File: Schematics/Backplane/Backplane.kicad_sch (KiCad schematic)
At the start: 0 parts

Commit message: First draft of schematic
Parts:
- added H1 (x2), H2 (x2), H3 (x2), H4 (x2): MountingHole, Footprints:Rod_Mounting_Hole_6.7564mm, symbol Mechanical:MountingHole
- added J1: Edge Connector (SLOT 1), footprints:AMPHENOL_10018784-10210TLF, symbol EdgeConnector:Stack Female Edge Connector
- added J2: Edge Connector (SLOT 2), footprints:AMPHENOL_10018784-10210TLF, symbol EdgeConnector:Stack Female Edge Connector
- added J3: Edge Connector (SLOT 3), footprints:AMPHENOL_10018784-10210TLF, symbol EdgeConnector:Stack Female Edge Connector
- added J4: Edge Connector (SLOT 4), footprints:AMPHENOL_10018784-10210TLF, symbol EdgeConnector:Stack Female Edge Connector
- added J5: Edge Connector (SLOT 5), footprints:AMPHENOL_10018784-10210TLF, symbol EdgeConnector:Stack Female Edge Connector
- added JP1: TOP_TERMINATION, symbol Jumper:Jumper_2_Bridged
- added JP2: BOT_TERMINATION, symbol Jumper:Jumper_2_Bridged
- added R1, R2: 120R, symbol Device:R
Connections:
- new net: JP2.1 (A), R2.1
- new net: JP1.1 (A), R1.1
- new net 3.3V_A: J1.A1 (3.3V_A), J1.A2 (3.3V_A), J2.A1 (3.3V_A), J2.A2 (3.3V_A), J3.A1 (3.3V_A), J3.A2 (3.3V_A), J4.A1 (3.3V_A), J4.A2 (3.3V_A), J5.A1 (3.3V_A), J5.A2 (3.3V_A)
- new net 3.3V_B: J1.A7 (3.3V_B), J1.A8 (3.3V_B), J2.A7 (3.3V_B), J2.A8 (3.3V_B), J3.A7 (3.3V_B), J3.A8 (3.3V_B), J4.A7 (3.3V_B), J4.A8 (3.3V_B), J5.A7 (3.3V_B), J5.A8 (3.3V_B)
- new net 5.0V_A: J1.A4 (5.0V_A), J1.A5 (5.0V_A), J2.A4 (5.0V_A), J2.A5 (5.0V_A), J3.A4 (5.0V_A), J3.A5 (5.0V_A), J4.A4 (5.0V_A), J4.A5 (5.0V_A), J5.A4 (5.0V_A), J5.A5 (5.0V_A)
- new net BATT_A: J1.B1 (BATT_A), J1.B2 (BATT_A), J1.B3 (BATT_A), J2.B1 (BATT_A), J2.B2 (BATT_A), J2.B3 (BATT_A), J3.B1 (BATT_A), J3.B2 (BATT_A), J3.B3 (BATT_A), J4.B1 (BATT_A), J4.B2 (BATT_A), J4.B3 (BATT_A), J5.B1 (BATT_A), J5.B2 (BATT_A), J5.B3 (BATT_A)
- new net BATT_B: J1.B7 (BATT_B), J1.B8 (BATT_B), J1.B9 (BATT_B), J2.B7 (BATT_B), J2.B8 (BATT_B), J2.B9 (BATT_B), J3.B7 (BATT_B), J3.B8 (BATT_B), J3.B9 (BATT_B), J4.B7 (BATT_B), J4.B8 (BATT_B), J4.B9 (BATT_B), J5.B7 (BATT_B), J5.B8 (BATT_B), J5.B9 (BATT_B)
- new net CAN_H: J1.B14 (CAN_H), J2.B14 (CAN_H), J3.B14 (CAN_H), J4.B14 (CAN_H), J5.B14 (CAN_H), JP1.2 (B), JP2.2 (B)
- new net CAN_L: J1.B13 (CAN_L), J2.B13 (CAN_L), J3.B13 (CAN_L), J4.B13 (CAN_L), J5.B13 (CAN_L), R1.2, R2.2
- new net GND1: J1.A3 (GND_A), J1.A6 (GND_A), J1.B4 (GND_A), J1.B5 (GND_A), J1.B6 (GND_A), J2.A3 (GND_A), J2.A6 (GND_A), J2.B4 (GND_A), J2.B5 (GND_A), J2.B6 (GND_A), J3.A3 (GND_A), J3.A6 (GND_A), J3.B4 (GND_A), J3.B5 (GND_A), J3.B6 (GND_A), J4.A3 (GND_A), J4.A6 (GND_A), J4.B4 (GND_A), J4.B5 (GND_A), J4.B6 (GND_A), J5.A3 (GND_A), J5.A6 (GND_A), J5.B4 (GND_A), J5.B5 (GND_A), J5.B6 (GND_A)
- new net GND2: J1.A12 (GND_B), J1.A9 (GND_B), J1.B10 (GND_B), J1.B11 (GND_B), J1.B12 (GND_B), J2.A12 (GND_B), J2.A9 (GND_B), J2.B10 (GND_B), J2.B11 (GND_B), J2.B12 (GND_B), J3.A12 (GND_B), J3.A9 (GND_B), J3.B10 (GND_B), J3.B11 (GND_B), J3.B12 (GND_B), J4.A12 (GND_B), J4.A9 (GND_B), J4.B10 (GND_B), J4.B11 (GND_B), J4.B12 (GND_B), J5.A12 (GND_B), J5.A9 (GND_B), J5.B10 (GND_B), J5.B11 (GND_B), J5.B12 (GND_B)
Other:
- note added: "1. WHAT SIZE MOUNTING HOLES? 2. EXPOSE DEBUG LEDS? 3. 4 LAYER OR 2 LAYER? 4. USE JLCPCB PCB ASSEMBLY?"
- note added: "CANBUS Termination"
- note added: "Mounting Holes"
- note added: "PASSTHROUGH?"

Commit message: Preliminary PCB design and layout
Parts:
- H1, H2, H3, H4: footprint Footprints:Rod_Mounting_Hole_6.7564mm -> MountingHole:MountingHole_3.2mm_M3_DIN965_Pad
- JP1, JP2: footprint (none) -> Jumper:SolderJumper-2_P1.3mm_Open_RoundedPad1.0x1.5mm
- R1, R2: footprint (none) -> Resistor_SMD:R_0805_2012Metric_Pad1.20x1.40mm_HandSolder
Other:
- note added: "1. EXPOSE DEBUG LEDS? 2. 4 LAYER OR 2 LAYER? 3. USE JLCPCB PCB ASSEMBLY? 4. NEED BETTER HOLE FOOTPRINTS?"
- note added: "DIMENSIONS NEED UPDATING"
- note removed: "1. WHAT SIZE MOUNTING HOLES? 2. EXPOSE DEBUG LEDS? 3. 4 LAYER OR 2 LAYER? 4. USE JLCPCB PCB ASSEMBLY?"
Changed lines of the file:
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@@
     (effects (font (size 1.27 1.27) (thickness 0.254) bold) (justify left bottom))
   )
-  (text "1. WHAT SIZE MOUNTING HOLES?\n2. EXPOSE DEBUG LEDS?\n3. 4 LAYER OR 2 LAYER?\n4. USE JLCPCB PCB ASSEMBLY?"
-    (at 21.59 166.37 0)
+  (text "DIMENSIONS NEED\nUPDATING" (at 308.61 185.42 0)
+    (effects (font (size 5 5) (thickness 1) bold) (justify left bottom))
+  )
+  (text "1. EXPOSE DEBUG LEDS?\n2. 4 LAYER OR 2 LAYER?\n3. USE JLCPCB PCB ASSEMBLY?\n4. NEED BETTER HOLE FOOTPRINTS?"
+    (at 146.05 154.94 0)
     (effects (font (size 2.5 2.5) (thickness 0.5) bold) (justify left bottom))
   )
@@
       (effects (font (size 1.27 1.27)) (justify left))
     )
-    (property "Footprint" "" (at 42.672 125.73 90)
+    (property "Footprint" "Resistor_SMD:R_0805_2012Metric_Pad1.20x1.40mm_HandSolder" (at 42.672 125.73 90)
       (effects (font (size 1.27 1.27)) hide)
     )
@@
       (effects (font (size 1.27 1.27)))
     )
-    (property "Footprint" "" (at 49.53 120.65 0)
+    (property "Footprint" "Jumper:SolderJumper-2_P1.3mm_Open_RoundedPad1.0x1.5mm" (at 49.53 120.65 0)
       (effects (font (size 1.27 1.27)) hide)
     )
@@
       (effects (font (size 1.27 1.27)) (justify left))
     )
-    (property "Footprint" "Footprints:Rod_Mounting_Hole_6.7564mm" (at 88.9 113.03 0)
+    (property "Footprint" "MountingHole:MountingHole_3.2mm_M3_DIN965_Pad" (at 88.9 113.03 0)
       (effects (font (size 1.27 1.27)) hide)
     )
@@
       (effects (font (size 1.27 1.27)) (justify left))
     )
-    (property "Footprint" "Footprints:Rod_Mounting_Hole_6.7564mm" (at 107.95 107.95 0)
+    (property "Footprint" "MountingHole:MountingHole_3.2mm_M3_DIN965_Pad" (at 107.95 107.95 0)
       (effects (font (size 1.27 1.27)) hide)
     )
@@
       (effects (font (size 1.27 1.27)) (justify left))
     )
-    (property "Footprint" "Footprints:Rod_Mounting_Hole_6.7564mm" (at 107.95 113.03 0)
+    (property "Footprint" "MountingHole:MountingHole_3.2mm_M3_DIN965_Pad" (at 107.95 113.03 0)
       (effects (font (size 1.27 1.27)) hide)
     )
@@
       (effects (font (size 1.27 1.27)) (justify left))
     )
-    (property "Footprint" "Footprints:Rod_Mounting_Hole_6.7564mm" (at 88.9 107.95 0)
+    (property "Footprint" "MountingHole:MountingHole_3.2mm_M3_DIN965_Pad" (at 88.9 107.95 0)
       (effects (font (size 1.27 1.27)) hide)
     )
@@
       (effects (font (size 1.27 1.27)) (justify left))
     )
-    (property "Footprint" "Footprints:Rod_Mounting_Hole_6.7564mm" (at 88.9 118.11 0)
+    (property "Footprint" "MountingHole:MountingHole_3.2mm_M3_DIN965_Pad" (at 88.9 118.11 0)
       (effects (font (size 1.27 1.27)) hide)
     )
@@
       (effects (font (size 1.27 1.27)))
     )
-    (property "Footprint" "" (at 49.53 102.87 0)
+    (property "Footprint" "Jumper:SolderJumper-2_P1.3mm_Open_RoundedPad1.0x1.5mm" (at 49.53 102.87 0)
       (effects (font (size 1.27 1.27)) hide)
     )
@@
       (effects (font (size 1.27 1.27)) (justify left))
     )
-    (property "Footprint" "" (at 42.672 107.95 90)
+    (property "Footprint" "Resistor_SMD:R_0805_2012Metric_Pad1.20x1.40mm_HandSolder" (at 42.672 107.95 90)
       (effects (font (size 1.27 1.27)) hide)
     )
@@
       (effects (font (size 1.27 1.27)) (justify left))
     )
-    (property "Footprint" "Footprints:Rod_Mounting_Hole_6.7564mm" (at 88.9 102.87 0)
+    (property "Footprint" "MountingHole:MountingHole_3.2mm_M3_DIN965_Pad" (at 88.9 102.87 0)
       (effects (font (size 1.27 1.27)) hide)
     )
@@
       (effects (font (size 1.27 1.27)) (justify left))
     )
-    (property "Footprint" "Footprints:Rod_Mounting_Hole_6.7564mm" (at 107.95 102.87 0)
+    (property "Footprint" "MountingHole:MountingHole_3.2mm_M3_DIN965_Pad" (at 107.95 102.87 0)
       (effects (font (size 1.27 1.27)) hide)
     )
@@
       (effects (font (size 1.27 1.27)) (justify left))
     )
-    (property "Footprint" "Footprints:Rod_Mounting_Hole_6.7564mm" (at 107.95 118.11 0)
-      (effects (font (size 1.27 1.27)) hide)
-    )
+    (property "Footprint" "MountingHole:MountingHole_3.2mm_M3_DIN965_Pad" (at 107.95 118.11 0)
+      (effects (font (size 1.27 1.27)) hide)
+    )

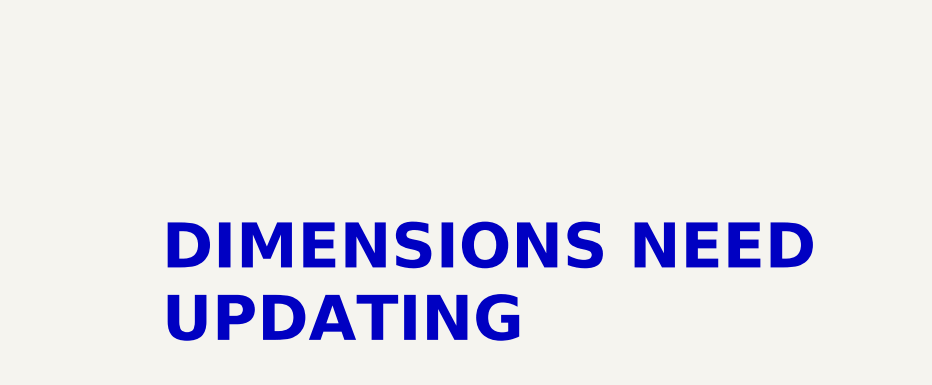
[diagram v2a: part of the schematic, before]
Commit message: Tweaked slot placement on PCB
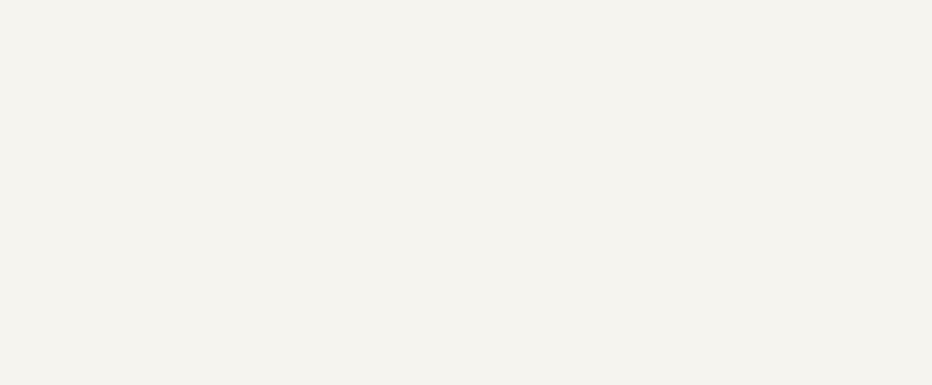
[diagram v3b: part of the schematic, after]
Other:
- note removed: "DIMENSIONS NEED UPDATING"

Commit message: Best attempt at 2-layer PCB (incomplete)
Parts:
- removed JP1: TOP_TERMINATION, Jumper:SolderJumper-2_P1.3mm_Open_RoundedPad1.0x1.5mm, symbol Jumper:Jumper_2_Bridged
- removed JP2: BOT_TERMINATION, Jumper:SolderJumper-2_P1.3mm_Open_RoundedPad1.0x1.5mm, symbol Jumper:Jumper_2_Bridged
- R1, R2: footprint Resistor_SMD:R_0805_2012Metric_Pad1.20x1.40mm_HandSolder -> Resistor_SMD:R_0603_1608Metric_Pad0.98x0.95mm_HandSolder
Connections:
- net CAN_H is gone; now on net CAN_P: J1.B14 (CAN_H), J2.B14 (CAN_H), J3.B14 (CAN_H), J4.B14 (CAN_H), J5.B14 (CAN_H)
- net CAN_P: now reaches R2.1
- net CAN_P: now also R1.1
- net CAN_L renamed CAN_N
- no-connect marks 0 -> 5
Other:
- note added: "2. 4 LAYER OR 2 LAYER? 3. USE JLCPCB PCB ASSEMBLY? 4. NEED BETTER HOLE FOOTPRINTS?"
- note added: "Added net labels so KiCAD sees them as differentials"
- note added: "Place on back of PCB"
- note added: "Place resistors at either end of CANBUS traces"
- note removed: "1. EXPOSE DEBUG LEDS? 2. 4 LAYER OR 2 LAYER? 3. USE JLCPCB PCB ASSEMBLY? 4. NEED BETTER HOLE FOOTPRINTS?"
- note removed: "PASSTHROUGH?"
- moved on the sheet: R1, R2

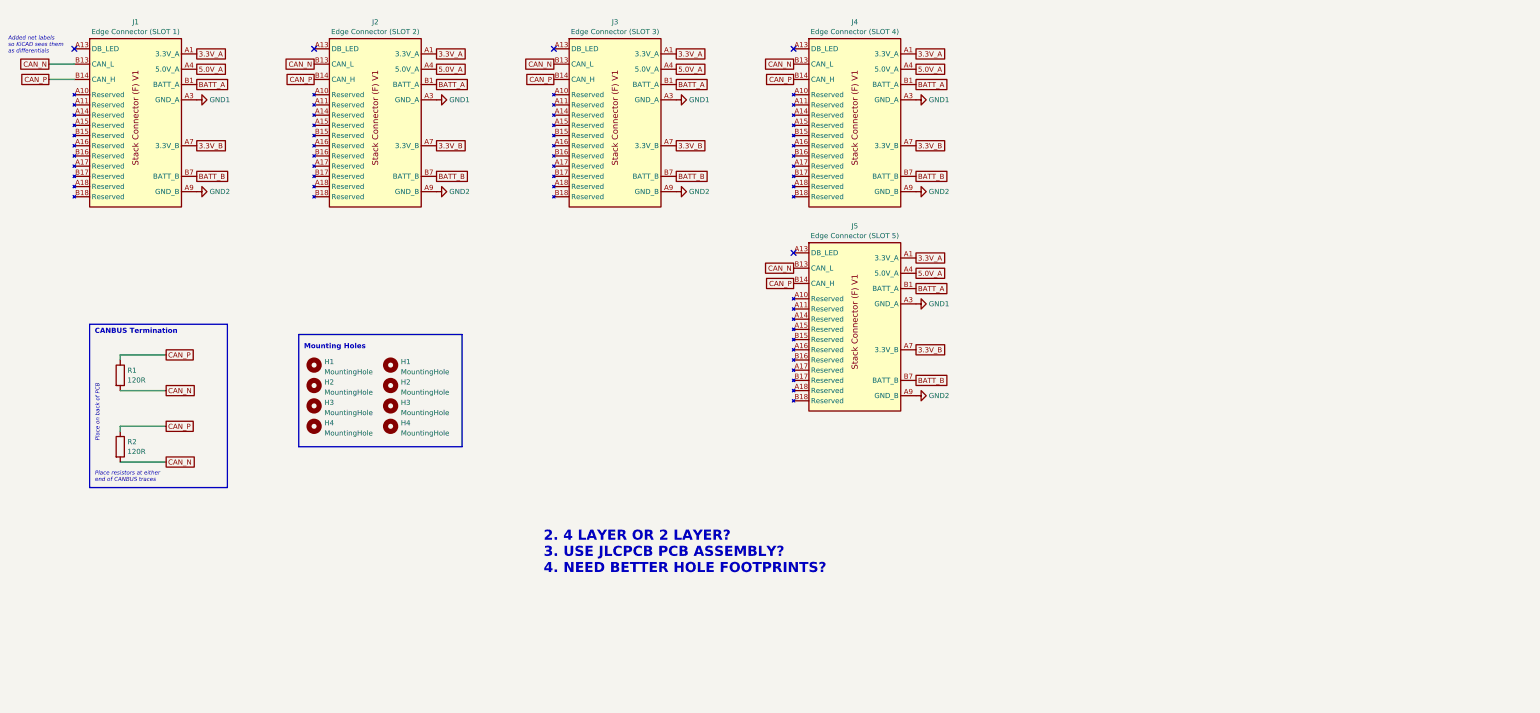
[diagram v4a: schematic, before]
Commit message: Completed PCB layout (2-layer). DRC Pass.
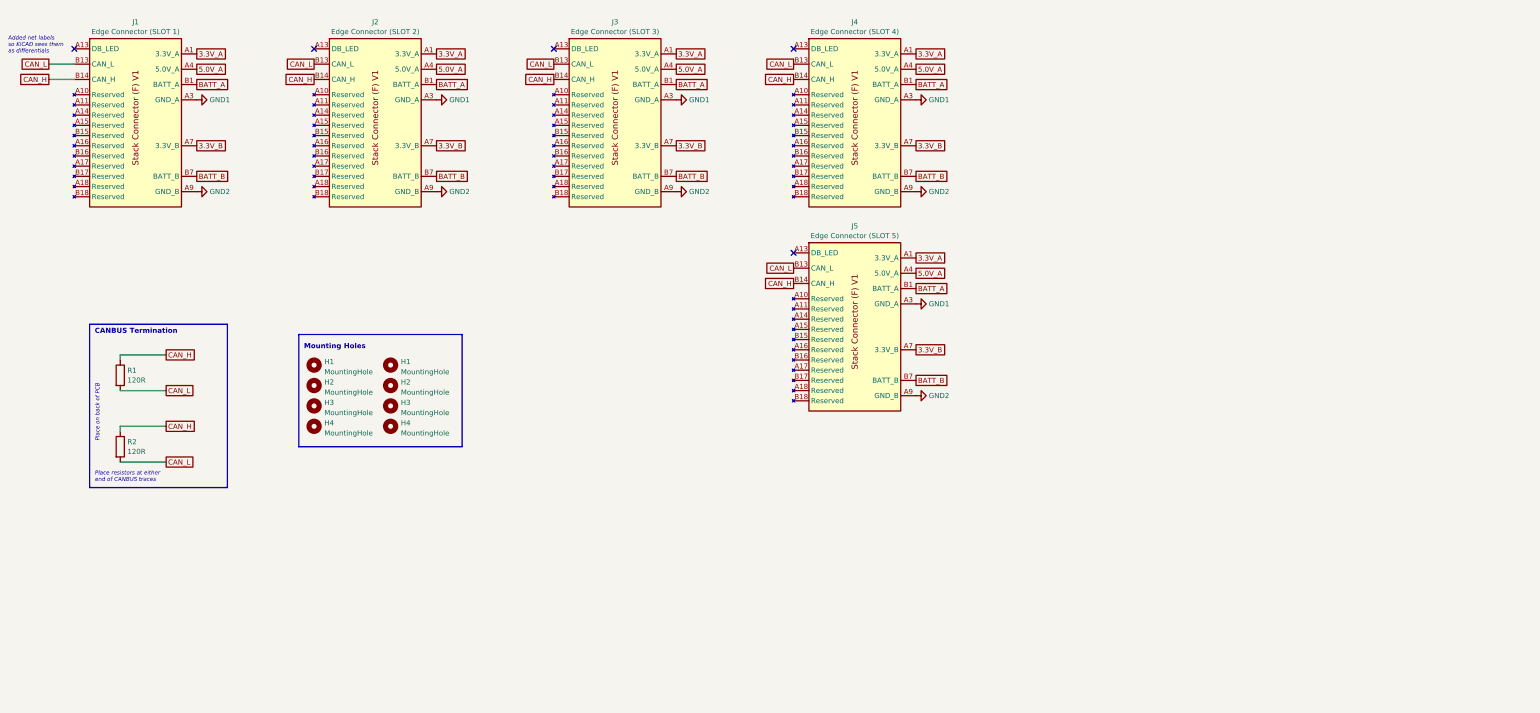
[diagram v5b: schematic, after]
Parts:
- H1, H2, H3, H4: footprint MountingHole:MountingHole_3.2mm_M3_DIN965_Pad -> MountingHole:MountingHole_3.2mm_M3_ISO14580_Pad; now left out of the parts list
- R1, R2: footprint Resistor_SMD:R_0603_1608Metric_Pad0.98x0.95mm_HandSolder -> Resistor_SMD:R_0805_2012Metric_Pad1.20x1.40mm_HandSolder; Digikey (none) -> A129738CT-ND
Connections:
- net CAN_N renamed CAN_L
- net CAN_P renamed CAN_H
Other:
- note removed: "2. 4 LAYER OR 2 LAYER? 3. USE JLCPCB PCB ASSEMBLY? 4. NEED BETTER HOLE FOOTPRINTS?"

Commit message: Cleaned up schematic
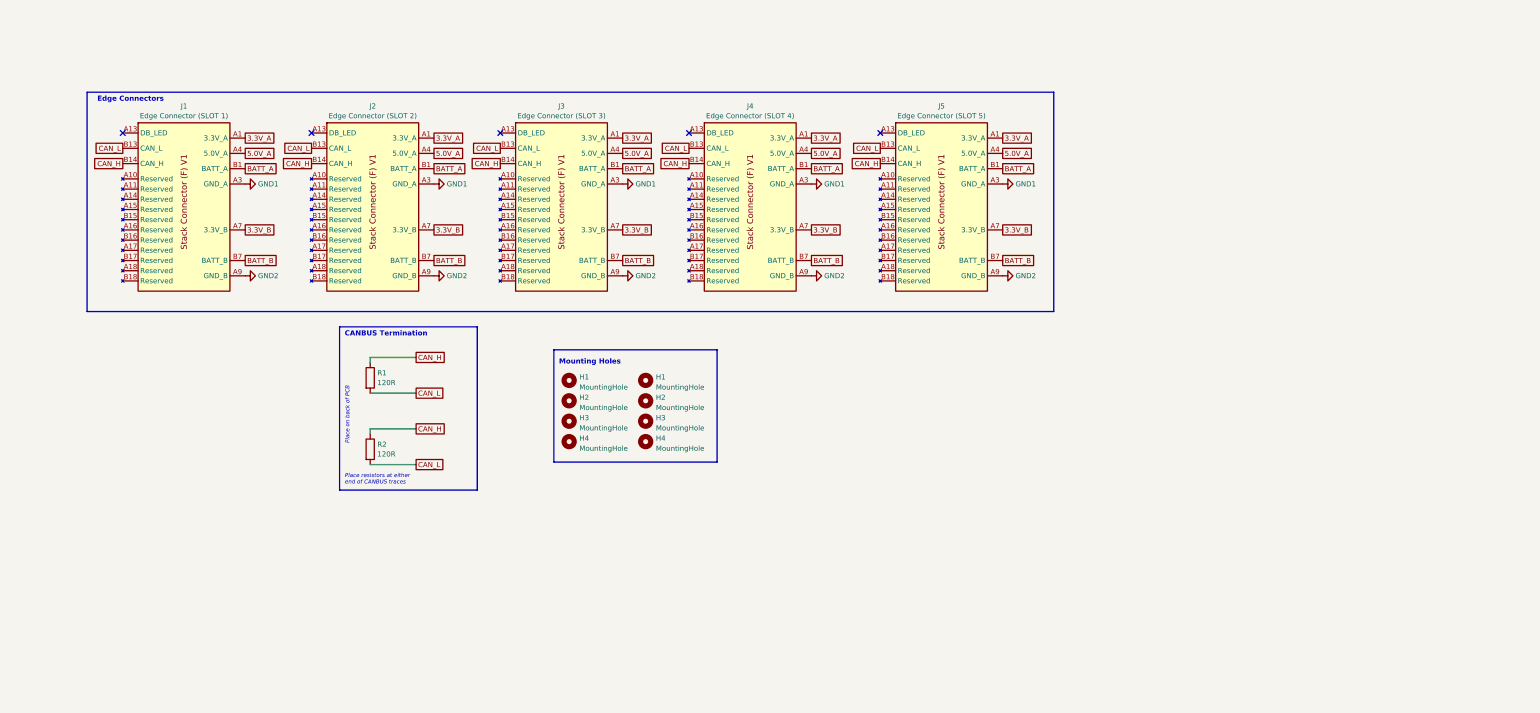
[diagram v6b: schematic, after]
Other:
- note added: "Edge Connectors"
- note removed: "Added net labels so KiCAD sees them as differentials"
- moved on the sheet: H1, H2, H3, H4, J1, J2, J3, J4, J5, R1, R2

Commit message: Added 6th module slot to schematic
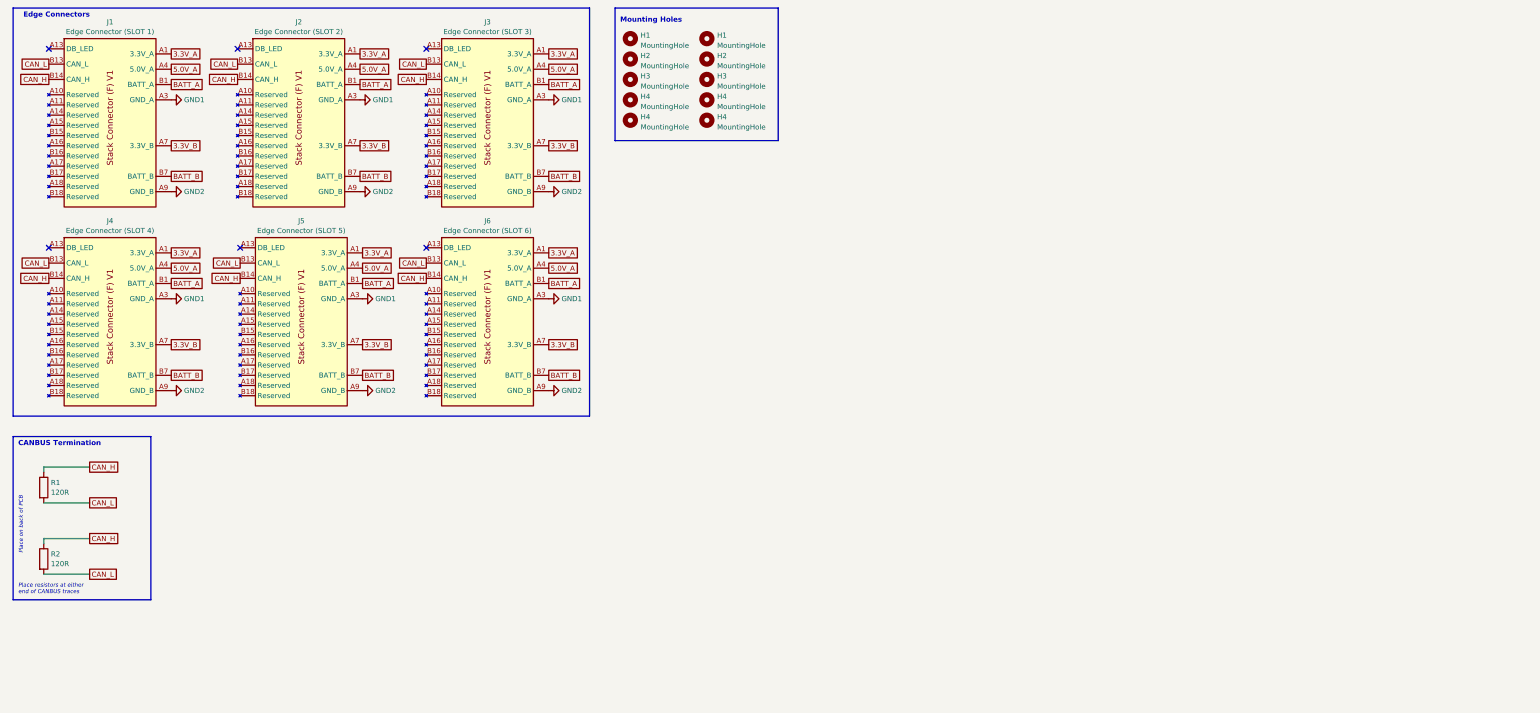
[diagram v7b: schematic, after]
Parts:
- added H4 (x2): MountingHole, MountingHole:MountingHole_3.2mm_M3_ISO14580_Pad, symbol Mechanical:MountingHole
- added J6: Edge Connector (SLOT 6), footprints:AMPHENOL_10018784-10210TLF, symbol EdgeConnector:Stack Female Edge Connector
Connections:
- net 3.3V_A: now also J6.A1 (3.3V_A), J6.A2 (3.3V_A)
- net 3.3V_B: now also J6.A7 (3.3V_B), J6.A8 (3.3V_B)
- net 5.0V_A: now also J6.A4 (5.0V_A), J6.A5 (5.0V_A)
- net BATT_A: now also J6.B1 (BATT_A), J6.B2 (BATT_A), J6.B3 (BATT_A)
- net BATT_B: now also J6.B7 (BATT_B), J6.B8 (BATT_B), J6.B9 (BATT_B)
- net CAN_H: now also J6.B14 (CAN_H)
- net CAN_L: now also J6.B13 (CAN_L)
- net GND1: now also J6.A3 (GND_A), J6.A6 (GND_A), J6.B4 (GND_A), J6.B5 (GND_A), J6.B6 (GND_A)
- net GND2: now also J6.A12 (GND_B), J6.A9 (GND_B), J6.B10 (GND_B), J6.B11 (GND_B), J6.B12 (GND_B)
- no-connect marks 5 -> 6
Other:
- title: QRET 23-24 SRAD Backplane PCB -> QRET 23-25 SRAD Backplane PCB
- moved on the sheet: H1, H2, H3, H4, J1, J2, J3, J4, J5, R1, R2
